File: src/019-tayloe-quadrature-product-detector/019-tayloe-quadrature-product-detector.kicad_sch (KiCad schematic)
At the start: 29 parts, among them J1 CONN, J2 CONN, J3 CONN, J4 CONN, J5 CONN, J6 CONN, J7 VCC, J8 VA, J9 VE, U1 74LVX74MTCX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

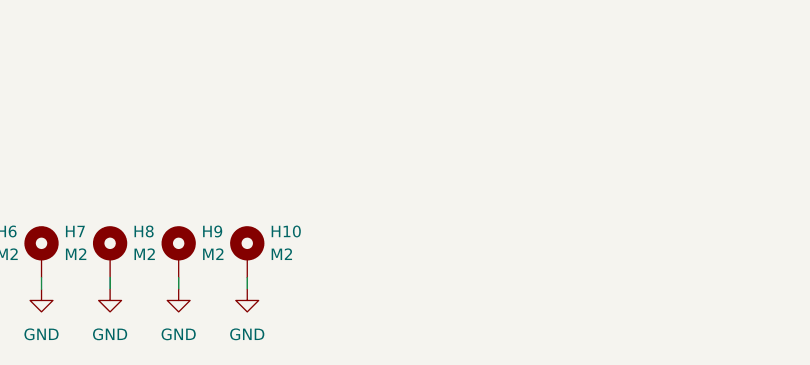
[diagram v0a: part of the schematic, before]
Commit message: Updating 019-tayloe-quadrature-product-detector for widing port spacing
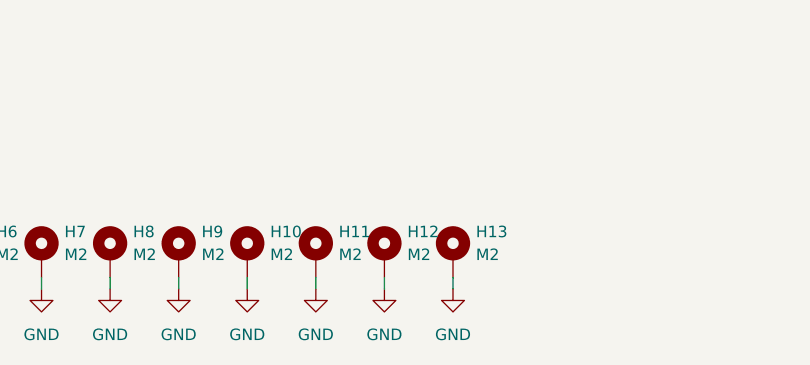
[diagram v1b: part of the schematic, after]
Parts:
- added H11, H12, H13: M2, modular-rf-bench-footprints:M2-hole, symbol Mechanical:MountingHole_Pad
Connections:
- net GND: now also H11.1, H12.1, H13.1
